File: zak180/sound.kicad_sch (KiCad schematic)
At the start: 19 parts, among them J4 Speaker, U11 74HC02, U16 74HC08, U17 LM386, U3 PSG_AY-3-8912

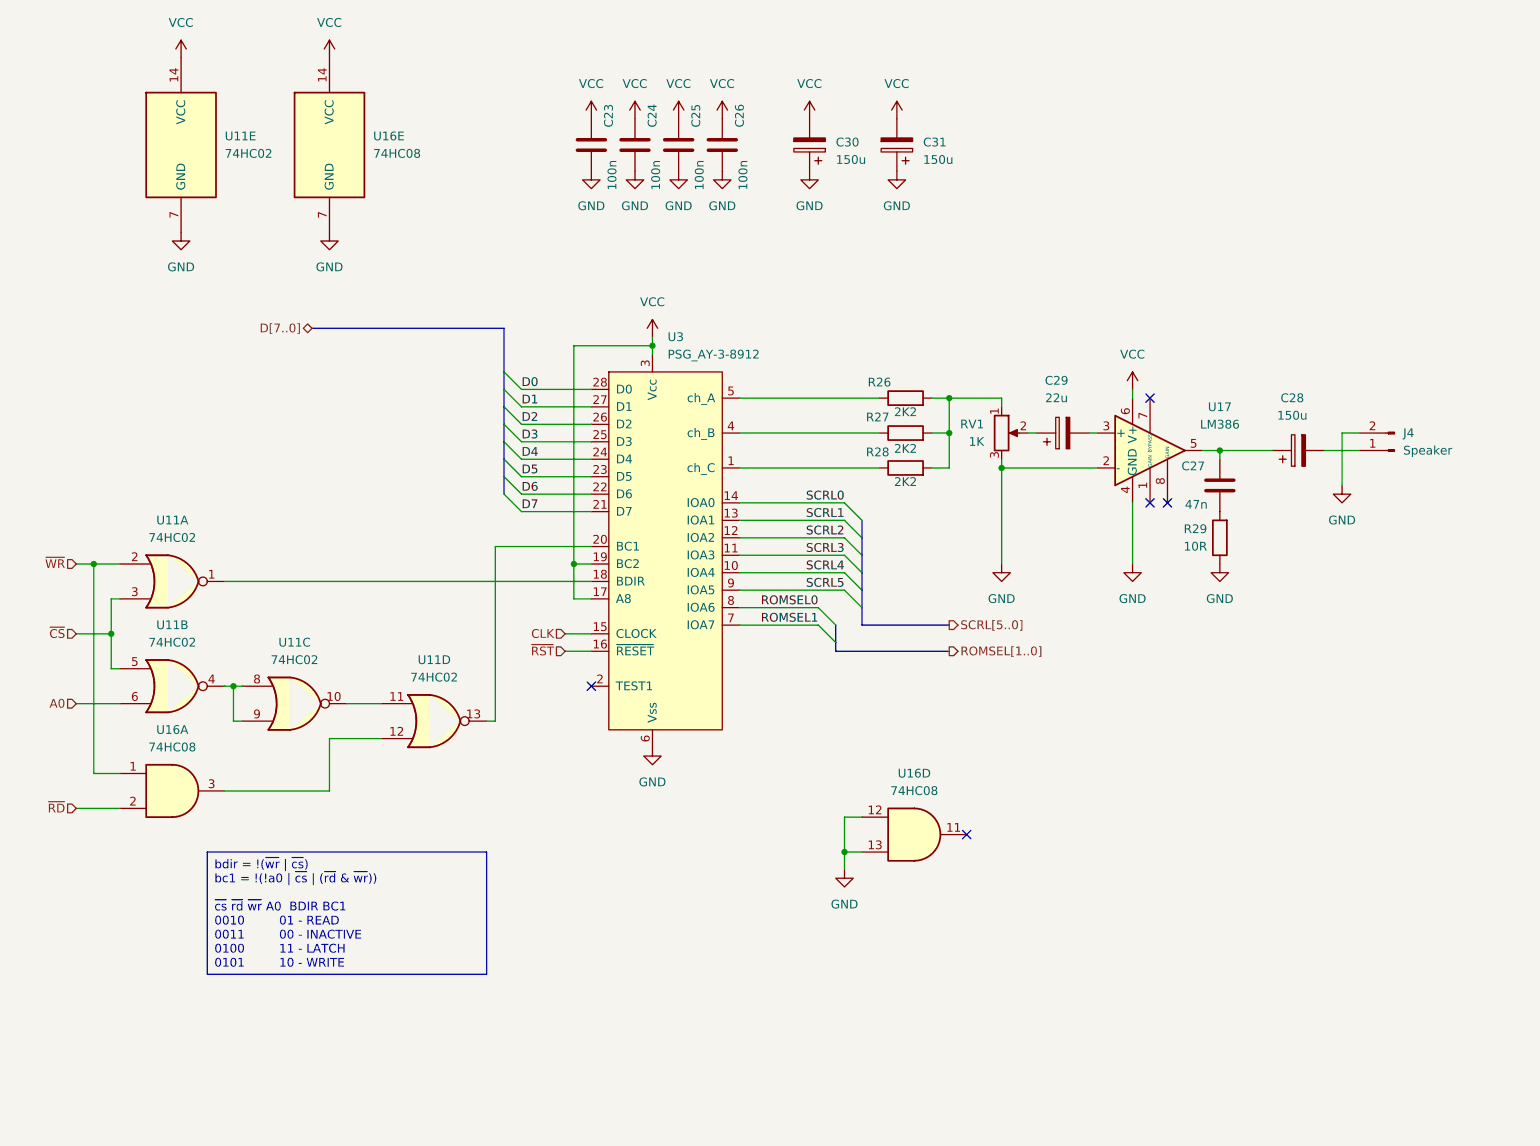
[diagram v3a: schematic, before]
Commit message: HW: Change RAM to static
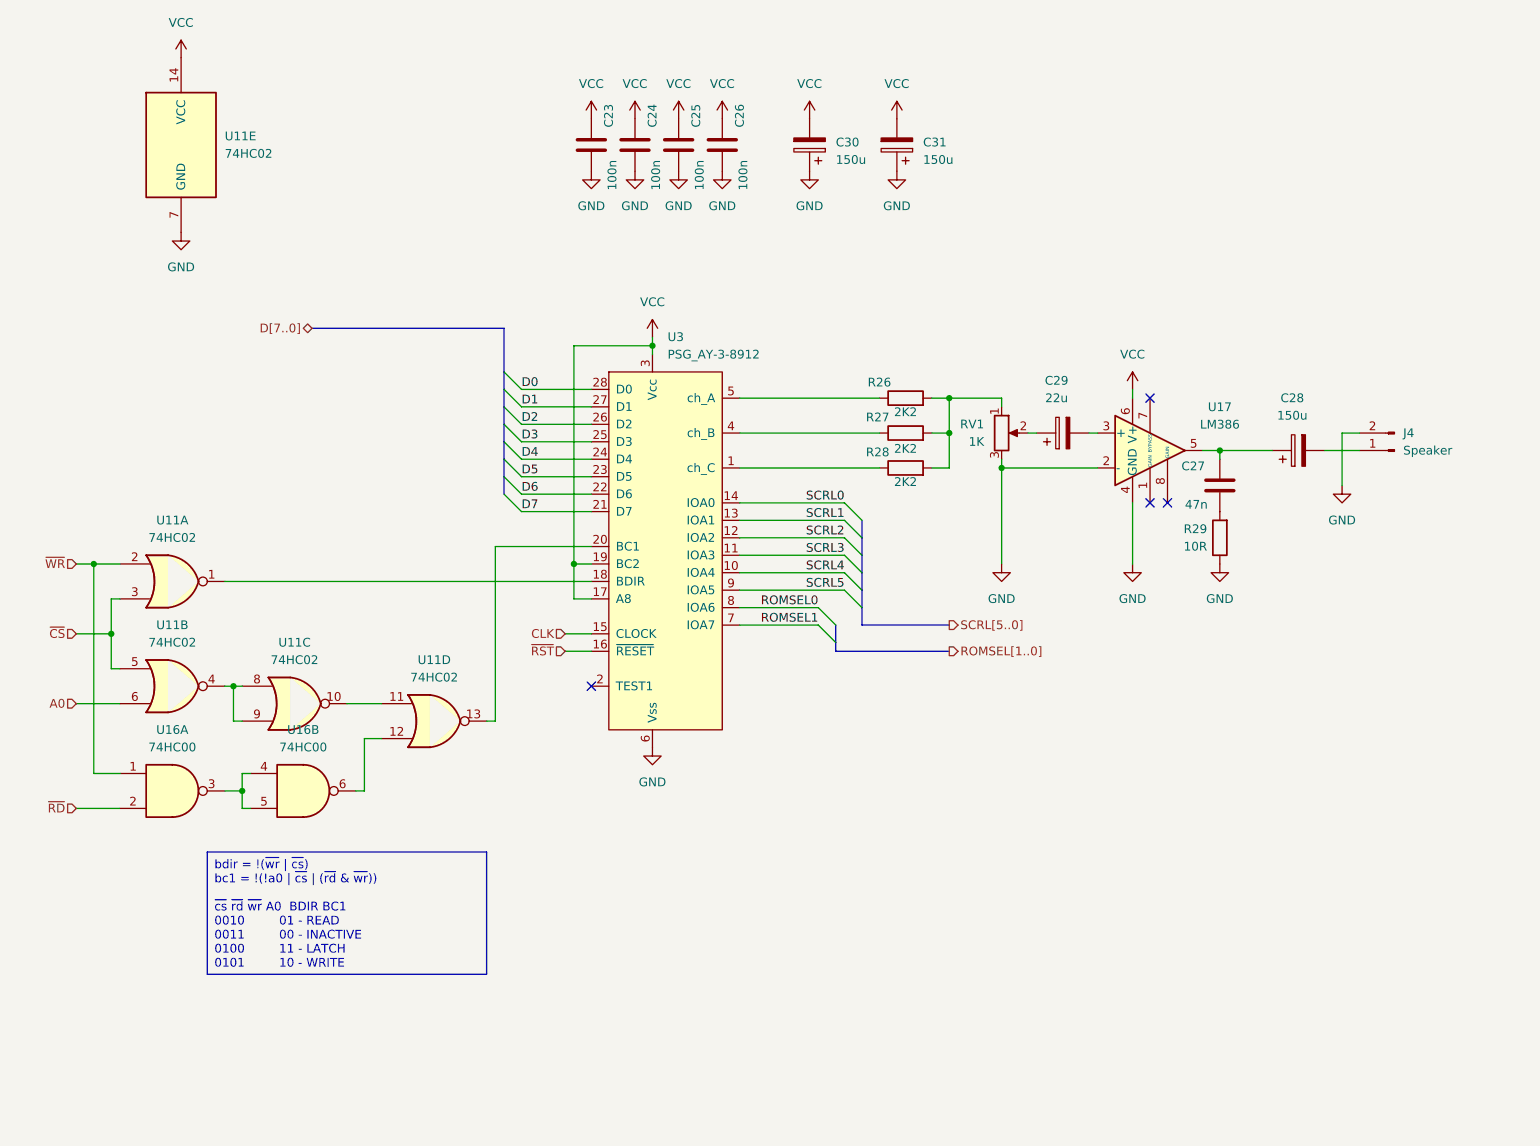
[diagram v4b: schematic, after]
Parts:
- removed U16: 74HC08, Package_DIP:DIP-14_W7.62mm, symbol 74xx:74LS08
- added U16: 74HC00, Package_DIP:DIP-14_W7.62mm, symbol 74xx:74HC00
- C28, C29, C30, C31: footprint (none) -> Capacitor_THT:CP_Radial_D10.0mm_P5.00mm
- RV1: footprint (none) -> PCM_Potentiometer_THT_AKL:Potentiometer_Vishay_T73YP_Vertical
- U17: footprint (none) -> Package_DIP:DIP-8_W7.62mm
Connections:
- net ~{RD}: now also U16.2
- net ~{WR}: now also U16.1
- net at U11.12: now also U16.6
- new net: U16.3, U16.4, U16.5
- no-connect marks 5 -> 4
